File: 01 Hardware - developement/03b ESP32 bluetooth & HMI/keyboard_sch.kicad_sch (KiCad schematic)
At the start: 42 parts, among them Q1 BC817, SW1 Rotary_Encoder_Switch, SW1 SW_Push_Dual, SW2 SW_Push_Dual, SW3 SW_Push_Dual, SW4 SW_Push_Dual, SW5 SW_Push_Dual

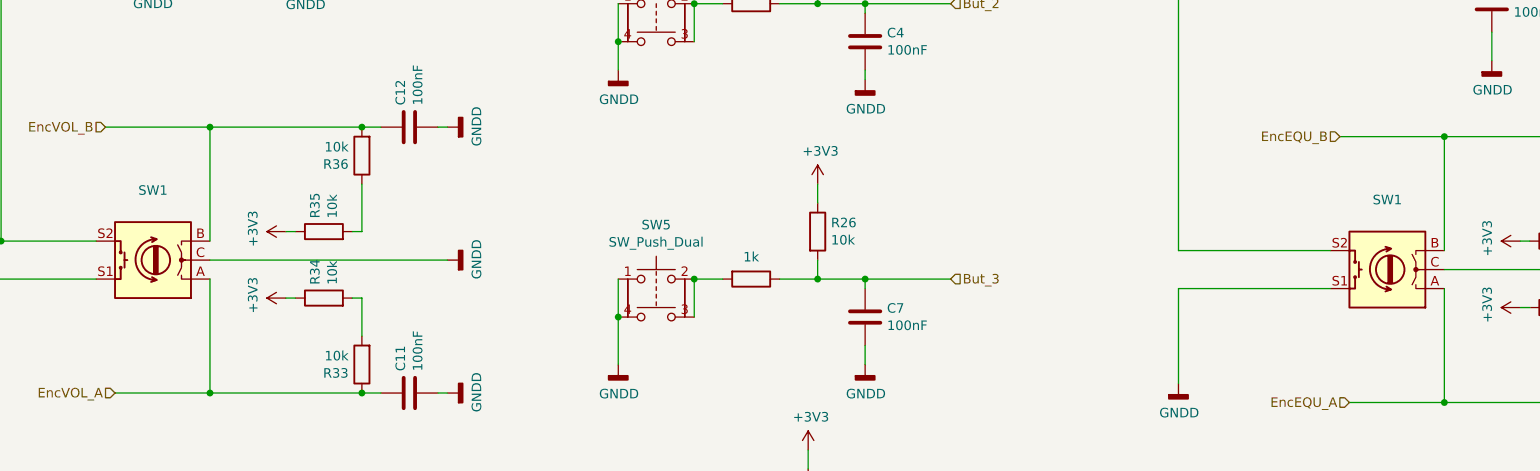
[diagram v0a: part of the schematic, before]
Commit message: errata dot. rezystora R57 i bootowania
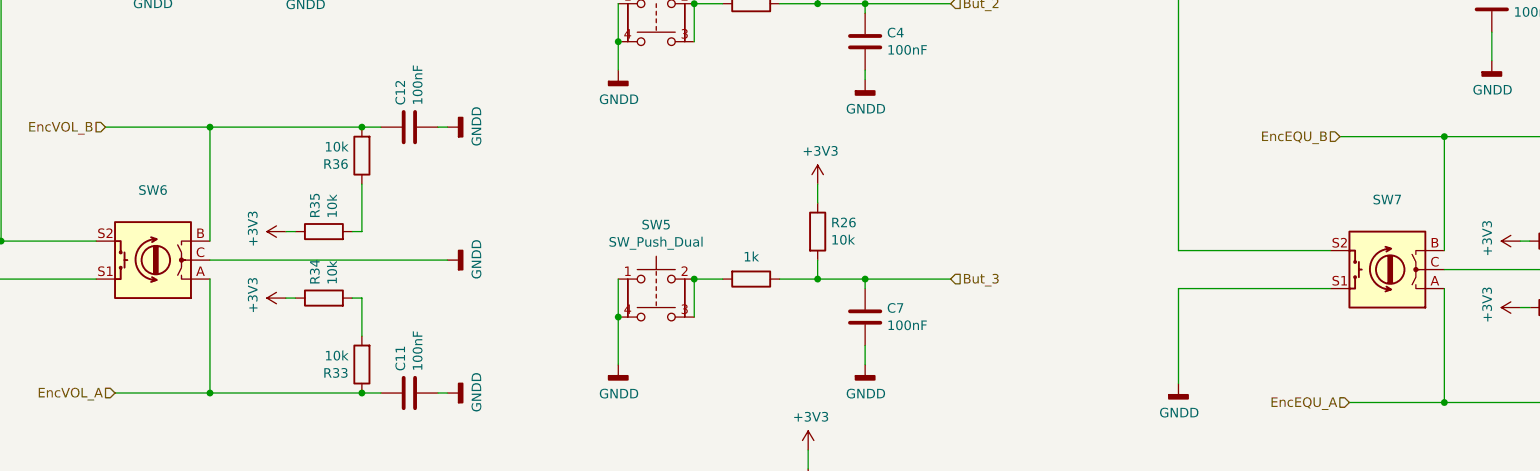
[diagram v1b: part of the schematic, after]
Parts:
- renumbered SW1 to SW6, SW1 to SW7

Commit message: Do poprwy jest schemat rotary encodera
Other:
- moved on the sheet: R29, R35
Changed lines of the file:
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@@
 		)
 	)
+	(polyline
+		(pts
+			(xy 67.31 106.68) (xy 86.36 106.68)
+		)
+		(stroke
+			(width 0.635)
+			(type solid)
+			(color 255 1 22 1)
+		)
+	)
 	(wire
 		(pts
@@
 	(wire
 		(pts
-			(xy 85.09 100.33) (xy 86.36 100.33)
+			(xy 85.09 99.06) (xy 86.36 99.06)
 		)
 		(stroke
@@
 		)
 	)
+	(polyline
+		(pts
+			(xy 64.77 111.76) (xy 69.85 114.3)
+		)
+		(stroke
+			(width 0.635)
+			(type solid)
+			(color 255 1 22 1)
+		)
+	)
 	(wire
 		(pts
@@
 		)
 	)
+	(polyline
+		(pts
+			(xy 64.77 114.3) (xy 69.85 116.84)
+		)
+		(stroke
+			(width 0.635)
+			(type solid)
+			(color 255 1 22 1)
+		)
+	)
 	(wire
 		(pts
@@
 	(wire
 		(pts
-			(xy 251.46 95.25) (xy 251.46 101.6)
+			(xy 251.46 95.25) (xy 251.46 100.33)
 		)
 		(stroke
@@
 		)
 	)
+	(polyline
+		(pts
+			(xy 228.6 92.71) (xy 233.68 95.25)
+		)
+		(stroke
+			(width 0.635)
+			(type solid)
+			(color 255 1 22 1)
+		)
+	)
 	(wire
 		(pts
@@
 		)
 	)
+	(polyline
+		(pts
+			(xy 63.5 91.44) (xy 68.58 93.98)
+		)
+		(stroke
+			(width 0.635)
+			(type solid)
+			(color 255 1 22 1)
+		)
+	)
 	(wire
 		(pts
-			(xy 76.2 100.33) (xy 77.47 100.33)
+			(xy 76.2 99.06) (xy 77.47 99.06)
 		)
 		(stroke
@@
 		)
 	)
+	(polyline
+		(pts
+			(xy 228.6 90.17) (xy 233.68 92.71)
+		)
+		(stroke
+			(width 0.635)
+			(type solid)
+			(color 255 1 22 1)
+		)
+	)
 	(wire
 		(pts
@@
 		)
 	)
+	(polyline
+		(pts
+			(xy 251.46 107.95) (xy 251.46 109.22)
+		)
+		(stroke
+			(width 0.635)
+			(type solid)
+			(color 255 1 22 1)
+		)
+	)
 	(wire
 		(pts
@@
 	(wire
 		(pts
-			(xy 250.19 101.6) (xy 251.46 101.6)
+			(xy 250.19 100.33) (xy 251.46 100.33)
 		)
 		(stroke
@@
 	(wire
 		(pts
-			(xy 241.3 101.6) (xy 242.57 101.6)
+			(xy 241.3 100.33) (xy 242.57 100.33)
 		)
 		(stroke
@@
 		)
 	)
+	(polyline
+		(pts
+			(xy 67.31 101.6) (xy 86.36 101.6)
+		)
+		(stroke
+			(width 0.635)
+			(type solid)
+			(color 255 1 22 1)
+		)
+	)
 	(wire
 		(pts
@@
 		)
 	)
+	(polyline
+		(pts
+			(xy 229.87 115.57) (xy 234.95 118.11)
+		)
+		(stroke
+			(width 0.635)
+			(type solid)
+			(color 255 1 22 1)
+		)
+	)
 	(wire
 		(pts
@@
 		)
 	)
+	(polyline
+		(pts
+			(xy 63.5 88.9) (xy 68.58 91.44)
+		)
+		(stroke
+			(width 0.635)
+			(type solid)
+			(color 255 1 22 1)
+		)
+	)
 	(wire
 		(pts
@@
 		)
 	)
+	(polyline
+		(pts
+			(xy 86.36 100.33) (xy 86.36 101.6)
+		)
+		(stroke
+			(width 0.635)
+			(type solid)
+			(color 255 1 22 1)
+		)
+	)
 	(wire
 		(pts
@@
 	(wire
 		(pts
-			(xy 86.36 93.98) (xy 86.36 100.33)
+			(xy 86.36 93.98) (xy 86.36 99.06)
 		)
 		(stroke
@@
 		)
 	)
+	(polyline
+		(pts
+			(xy 229.87 113.03) (xy 234.95 115.57)
+		)
+		(stroke
+			(width 0.635)
+			(type solid)
+			(color 255 1 22 1)
+		)
+	)
+	(polyline
+		(pts
+			(xy 232.41 107.95) (xy 251.46 107.95)
+		)
+		(stroke
+			(width 0.635)
+			(type solid)
+			(color 255 1 22 1)
+		)
+	)
 	(wire
 		(pts
@@
 		)
 	)
+	(polyline
+		(pts
+			(xy 86.36 106.68) (xy 86.36 107.95)
+		)
+		(stroke
+			(width 0.635)
+			(type solid)
+			(color 255 1 22 1)
+		)
+	)
 	(wire
 		(pts
@@
 		)
 	)
+	(polyline
+		(pts
+			(xy 232.41 102.87) (xy 251.46 102.87)
+		)
+		(stroke
+			(width 0.635)
+			(type solid)
+			(color 255 1 22 1)
+		)
+	)
 	(wire
 		(pts
@@
 		)
 	)
+	(polyline
+		(pts
+			(xy 251.46 101.6) (xy 251.46 102.87)
+		)
+		(stroke
+			(width 0.635)
+			(type solid)
+			(color 255 1 22 1)
+		)
+	)
 	(wire
 		(pts
@@
 	(symbol
 		(lib_id "Device:R")
-		(at 246.38 101.6 90)
+		(at 246.38 100.33 90)
 		(unit 1)
 		(exclude_from_sim no)
@@
 		(dnp no)
 		(property "Reference" "R29"
-			(at 245.2116 99.822 0)
+			(at 245.2116 98.552 0)
 			(effects
 				(font
@@
 		)
 		(property "Value" "10k"
-			(at 247.523 99.822 0)
+			(at 247.523 98.552 0)
 			(effects
 				(font
@@
 		)
 		(property "Footprint" "Resistor_SMD:R_0603_1608Metric"
-			(at 246.38 103.378 90)
+			(at 246.38 102.108 90)
 			(effects
 				(font
@@
 		)
 		(property "Datasheet" "~"
-			(at 246.38 101.6 0)
+			(at 246.38 100.33 0)
 			(effects
 				(font
@@
 		)
 		(property "Description" ""
-			(at 246.38 101.6 0)
+			(at 246.38 100.33 0)
 			(effects
 				(font
@@
 		)
 		(property "TME no." "RC0603FR-1310KL"
-			(at 246.38 101.6 0)
+			(at 246.38 100.33 0)
 			(effects
 				(font
@@
 	(symbol
 		(lib_id "power:+3V3")
-		(at 241.3 101.6 90)
+		(at 241.3 100.33 90)
 		(unit 1)
 		(exclude_from_sim no)
@@
 		(dnp no)
 		(property "Reference" "#PWR039"
-			(at 245.11 101.6 0)
+			(at 245.11 100.33 0)
 			(effects
 				(font
@@
 		)
 		(property "Value" "+3V3"
-			(at 236.9058 101.219 0)
+			(at 236.9058 99.949 0)
 			(effects
 				(font
@@
 		)
 		(property "Footprint" ""
-			(at 241.3 101.6 0)
+			(at 241.3 100.33 0)
 			(effects
 				(font
@@
 		)
 		(property "Datasheet" ""
-			(at 241.3 101.6 0)
+			(at 241.3 100.33 0)
 			(effects
 				(font
@@
 		)
 		(property "Description" ""
-			(at 241.3 101.6 0)
+			(at 241.3 100.33 0)
 			(effects
 				(font
@@
 	(symbol
 		(lib_id "Device:R")
-		(at 81.28 100.33 90)
+		(at 81.28 99.06 90)
 		(unit 1)
 		(exclude_from_sim no)
@@
 		(dnp no)
 		(property "Reference" "R35"
-			(at 80.1116 98.552 0)
+			(at 80.1116 97.282 0)
 			(effects
 				(font
@@
 		)
 		(property "Value" "10k"
-			(at 82.423 98.552 0)
+			(at 82.423 97.282 0)
 			(effects
 				(font
@@
 		)
 		(property "Footprint" "Resistor_SMD:R_0603_1608Metric"
-			(at 81.28 102.108 90)
+			(at 81.28 100.838 90)
 			(effects
 				(font
@@
 		)
 		(property "Datasheet" "~"
-			(at 81.28 100.33 0)
+			(at 81.28 99.06 0)
 			(effects
 				(font
@@
 		)
 		(property "Description" ""
-			(at 81.28 100.33 0)
+			(at 81.28 99.06 0)
 			(effects
 				(font
@@
 		)
 		(property "TME no." "RC0603FR-1310KL"
-			(at 81.28 100.33 0)
+			(at 81.28 99.06 0)
 			(effects
 				(font
@@
 	(symbol
 		(lib_id "power:+3V3")
-		(at 76.2 100.33 90)
+		(at 76.2 99.06 90)
 		(unit 1)
 		(exclude_from_sim no)
@@
 		(dnp no)
 		(property "Reference" "#PWR046"
-			(at 80.01 100.33 0)
+			(at 80.01 99.06 0)
 			(effects
 				(font
@@
 		)
 		(property "Value" "+3V3"
-			(at 71.8058 99.949 0)
+			(at 71.8058 98.679 0)
 			(effects
 				(font
@@
 		)
 		(property "Footprint" ""
-			(at 76.2 100.33 0)
+			(at 76.2 99.06 0)
 			(effects
 				(font
@@
 		)
 		(property "Datasheet" ""
-			(at 76.2 100.33 0)
+			(at 76.2 99.06 0)
 			(effects
 				(font
@@
 		)
 		(property "Description" ""
-			(at 76.2 100.33 0)
+			(at 76.2 99.06 0)
 			(effects
 				(font
